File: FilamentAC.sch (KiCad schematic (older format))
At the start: 4 parts, among them U1201 SN74LVC1G04, U1202 SI9986/7

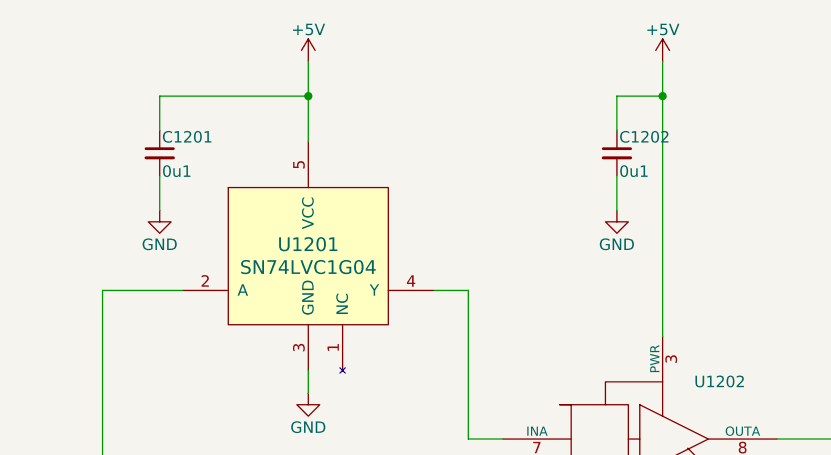
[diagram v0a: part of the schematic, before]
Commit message: switching to more convenient notation of values, e.g. 100K instead of 0M1
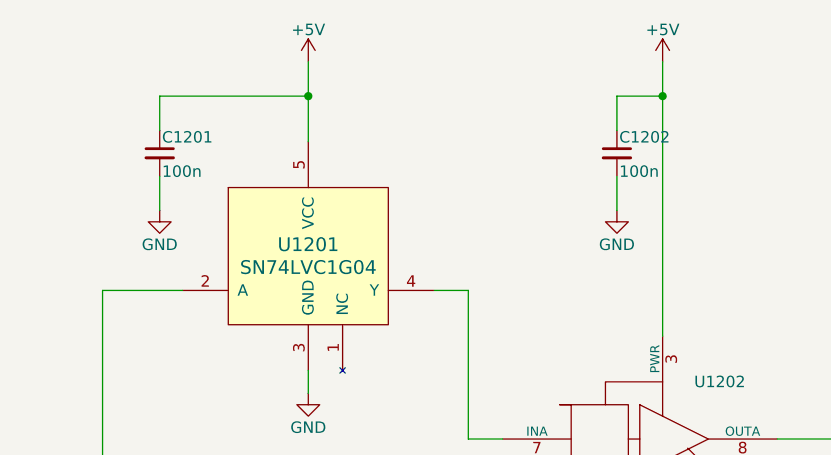
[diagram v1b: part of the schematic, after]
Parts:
- C1201, C1202: value 0u1 -> 100n
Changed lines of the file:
@@
 P 4000 1250
 F 0 "C1202" H 4010 1320 50  0000 L CNN
-F 1 "0u1" H 4010 1170 50  0000 L CNN
+F 1 "100n" H 4010 1170 50  0000 L CNN
 F 2 "Capacitors_SMD:C_0805_HandSoldering" H 4000 1250 50  0001 C CNN
 F 3 "" H 4000 1250 50  0001 C CNN
@@
 P 2000 1250
 F 0 "C1201" H 2010 1320 50  0000 L CNN
-F 1 "0u1" H 2010 1170 50  0000 L CNN
+F 1 "100n" H 2010 1170 50  0000 L CNN
 F 2 "Capacitors_SMD:C_0805_HandSoldering" H 2000 1250 50  0001 C CNN
 F 3 "" H 2000 1250 50  0001 C CNN
